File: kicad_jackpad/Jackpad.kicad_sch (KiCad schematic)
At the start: 43 parts, among them J1 USB_C_Receptacle, J2 XT 30, J3 4pin connector, SW1 SW_Push, SW2 SW_Push, SW3 SPDT slide switch, 3A min, U1 ESP32-S3-WROOM-1, U2 AMS1117-3.3, U3 AS5600, U4 TPS568215RNN

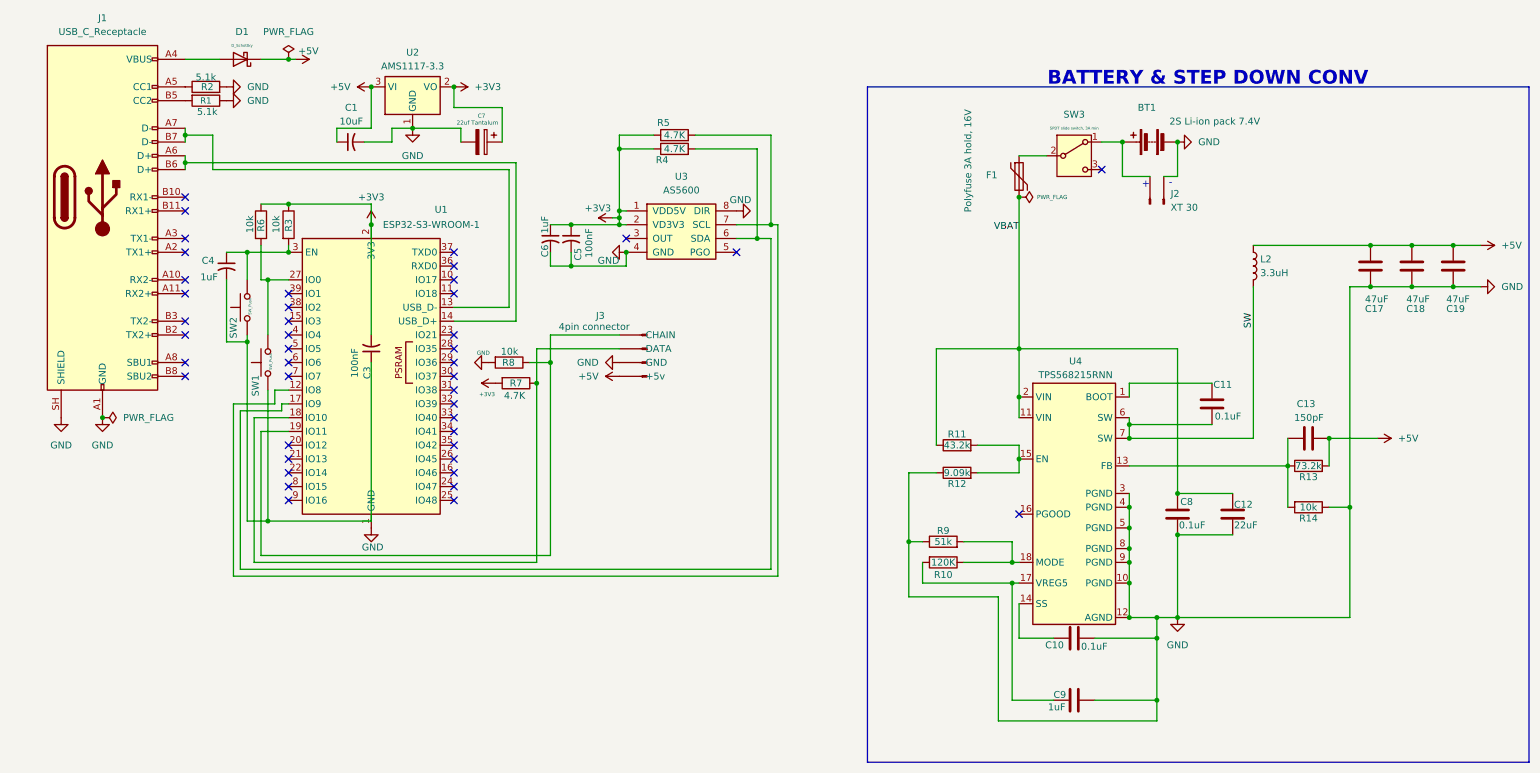
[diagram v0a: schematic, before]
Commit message: fixed step down converter wiring
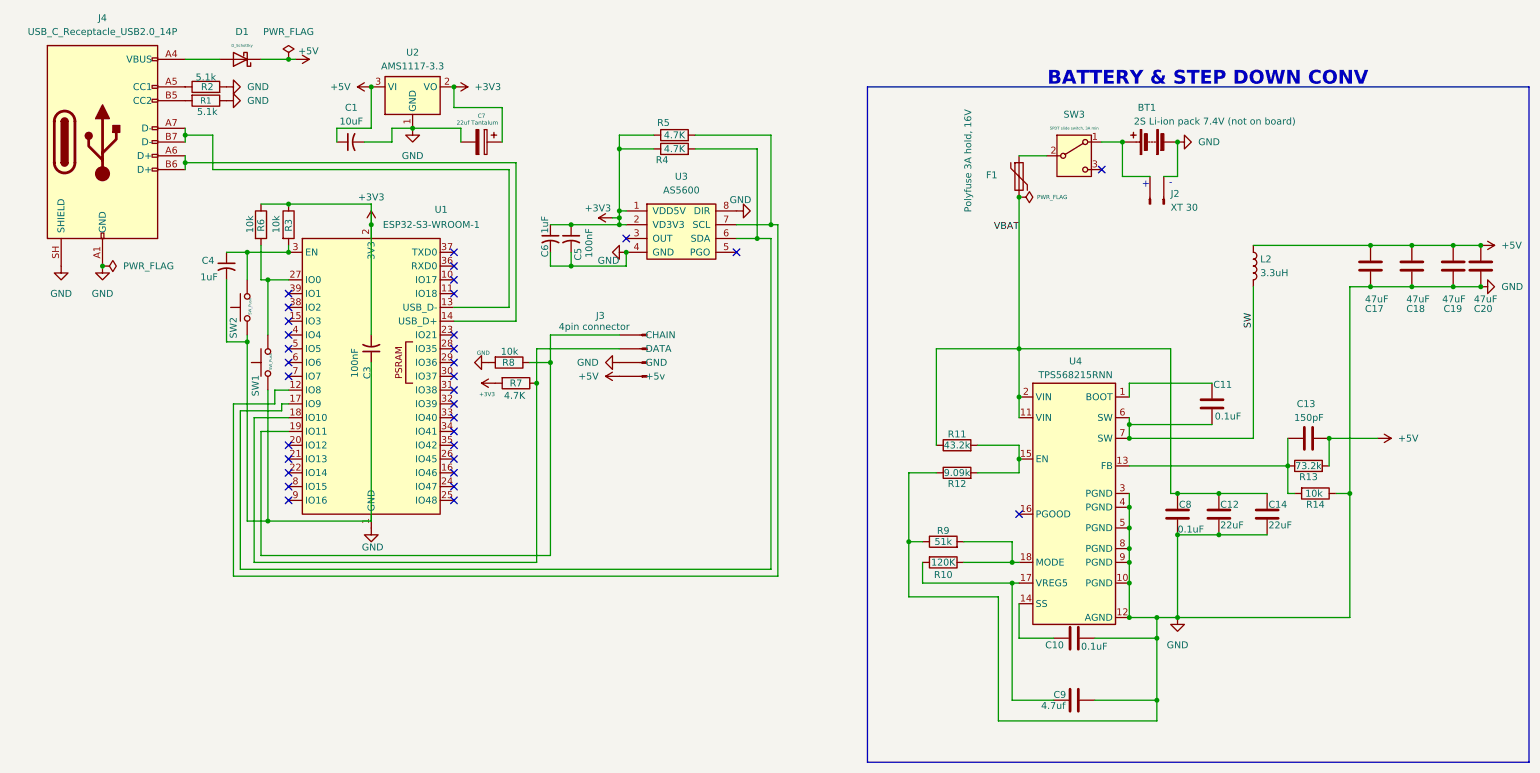
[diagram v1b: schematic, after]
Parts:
- removed J1: USB_C_Receptacle, symbol Connector:USB_C_Receptacle
- added C14: 22uF, symbol Device:C
- added C20: 47uF, symbol Device:C
- added J4: USB_C_Receptacle_USB2.0_14P, symbol Connector:USB_C_Receptacle_USB2.0_14P
- BT1: value 2S Li-ion pack 7.4V -> 2S Li-ion pack 7.4V (not on board)
- C9: value 1uF -> 4.7uf
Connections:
- net +5V: now also C20.2
- net GND: now also C14.2, C20.1, J4.A1 (GND), J4.A12 (GND), J4.B1 (GND), J4.B12 (GND), J4.SH (SHIELD)
- net VBAT: now also C14.1
- net at D1.2 (A): now also J4.A4 (VBUS), J4.A9 (VBUS), J4.B4 (VBUS), J4.B9 (VBUS)
- net at R2.1: now also J4.A5 (CC1)
- net at U1.14 (USB_D+): now also J4.A6 (D+), J4.B6 (D+)
- net at U1.13 (USB_D-): now also J4.A7 (D-), J4.B7 (D-)
- net at R1.2: now also J4.B5 (CC2)
- no-connect marks 43 -> 33
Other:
- moved on the sheet: C12, R14
